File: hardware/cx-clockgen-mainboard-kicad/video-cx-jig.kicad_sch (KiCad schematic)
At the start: 10 parts, among them J1 Conn_Coaxial, J2 Conn_01x01_Pin, J3 Conn_01x01_Pin, J4 Conn_01x01_Pin, J5 Conn_01x01_Pin

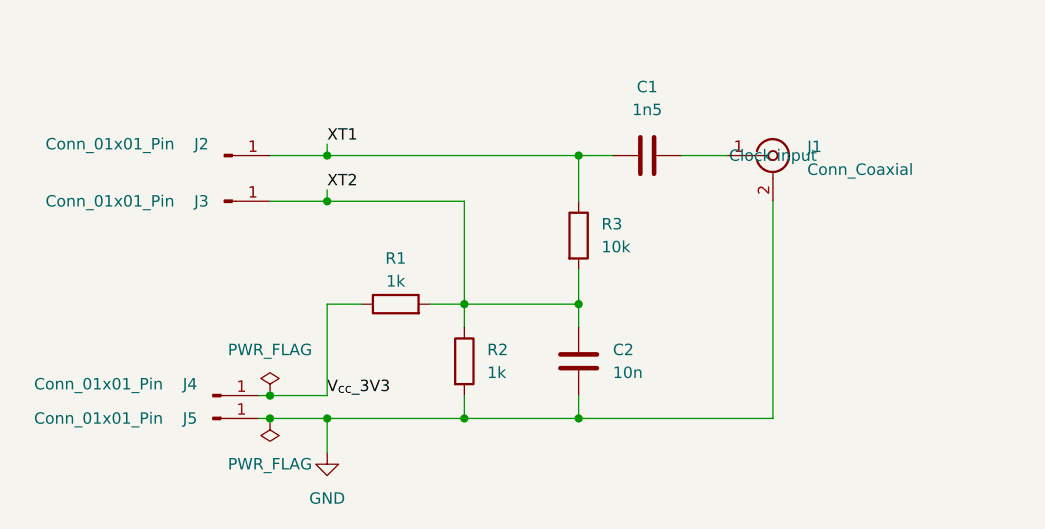
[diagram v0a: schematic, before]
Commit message: Remove obsolete KiCad project files for the clock generator main board, including DRC, ERC, DRU, PCB, schematic, and project configuration files. Updated the CX Jig project files with new author and company details, modified component properties, and adjusted net definitions for improved clarity and organization.
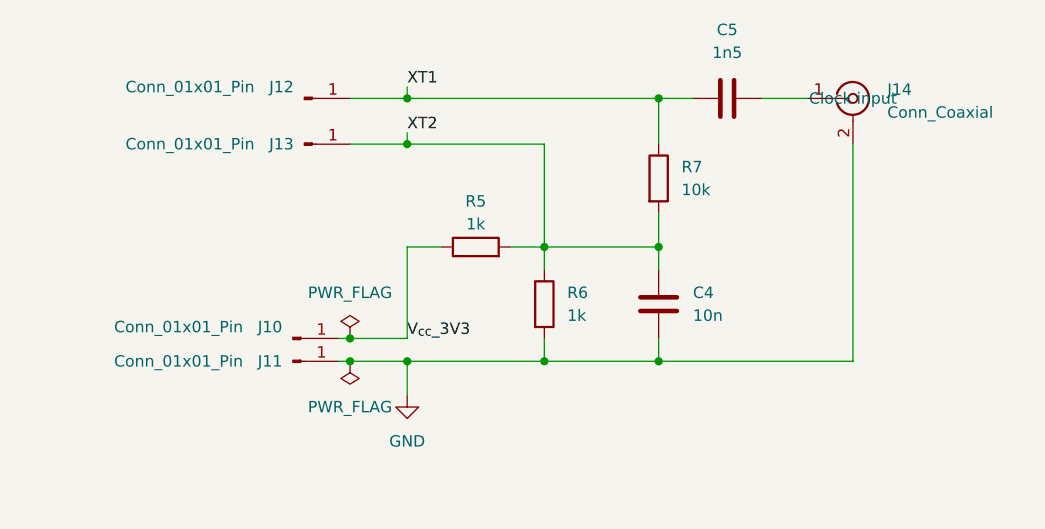
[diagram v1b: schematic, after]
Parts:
- renumbered C2 to C4, C1 to C5, J4 to J10, J5 to J11, J2 to J12, J3 to J13, J1 to J14, R1 to R5, R2 to R6, R3 to R7
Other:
- company: ${proj-author} -> ${proj-company}
- title: ${proj-title} -> Video CX Jig
- moved on the sheet: C4, C5, J10, J11, J12, J13, J14, R5, R6, R7
